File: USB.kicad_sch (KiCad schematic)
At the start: 34 parts, among them J1 USB_C_Receptable_USB2.0, U4 AP2141WG-7

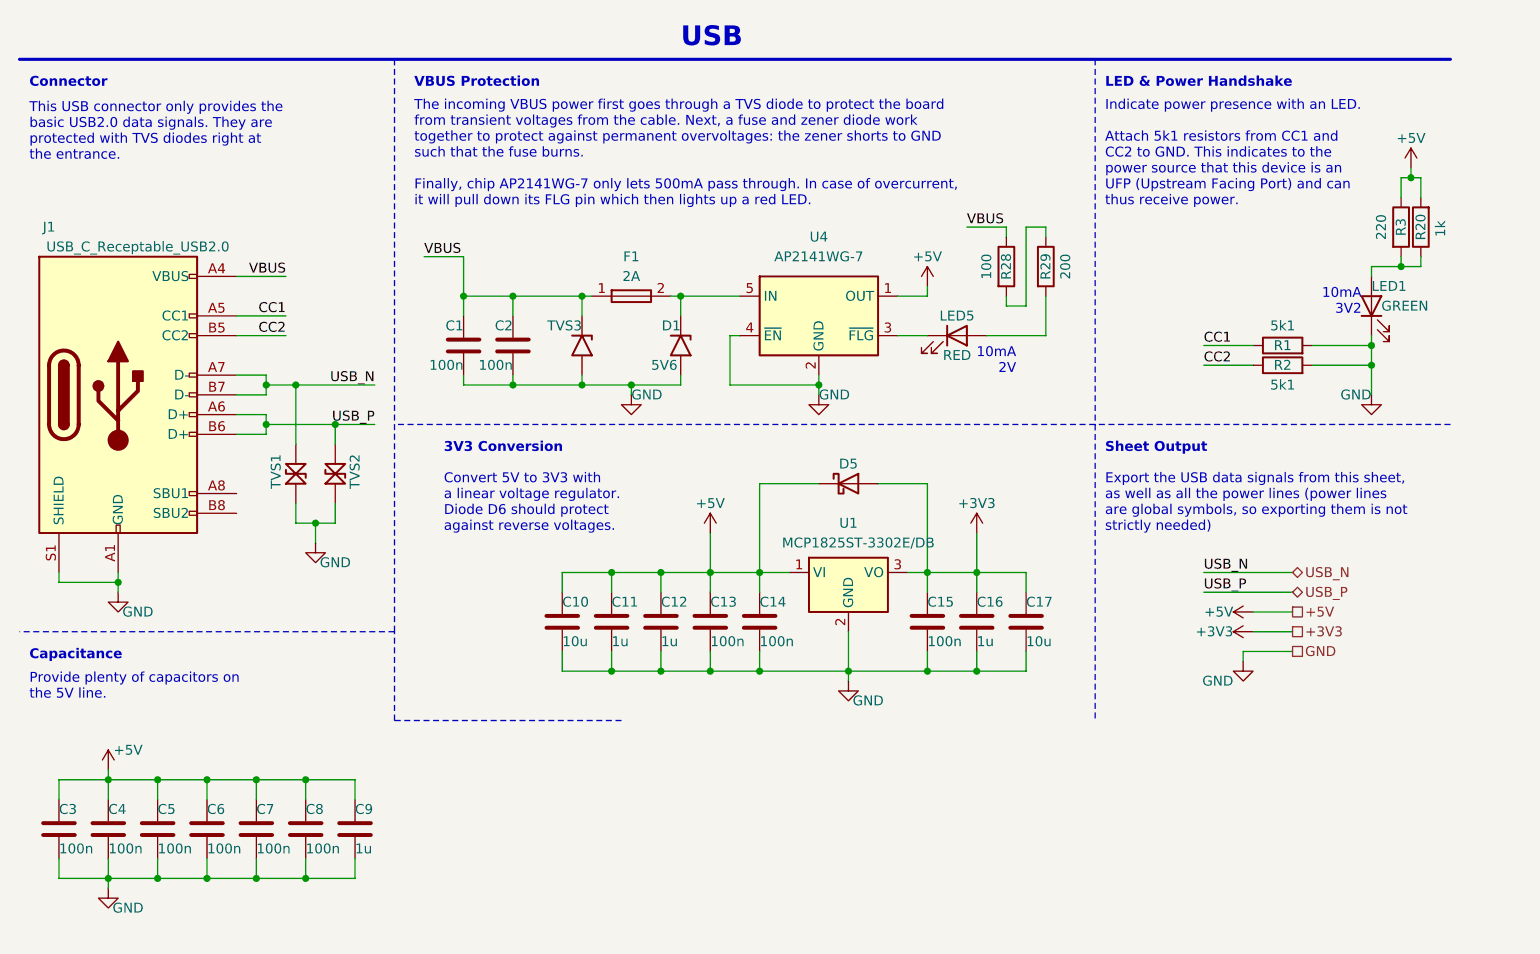
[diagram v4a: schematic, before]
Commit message: Renumber designators and draw new silkscreen
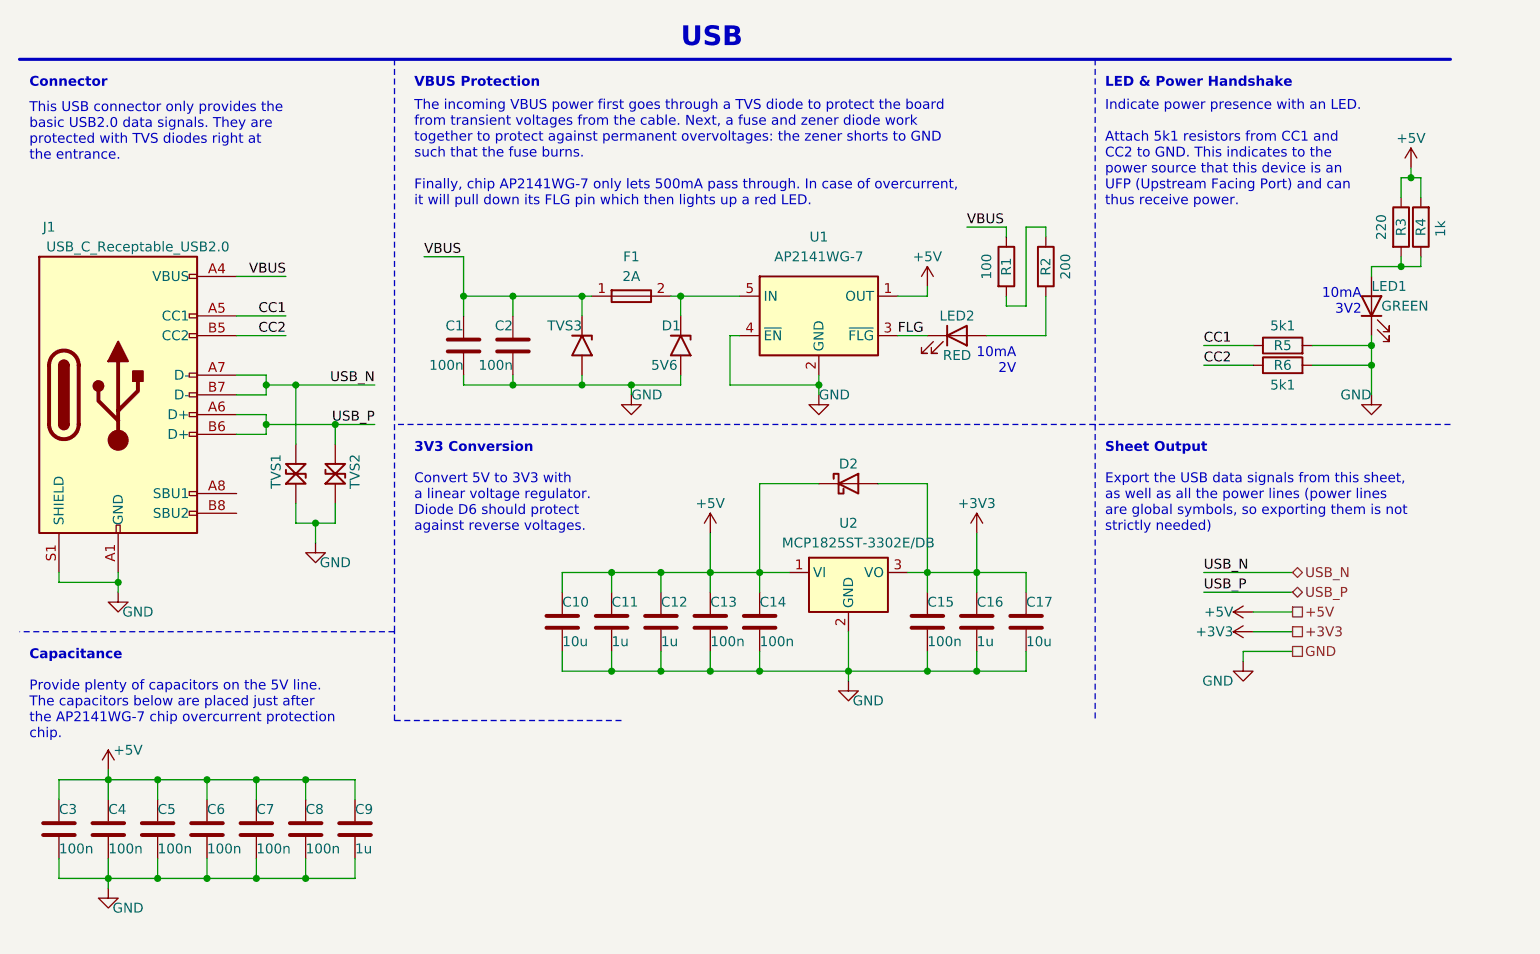
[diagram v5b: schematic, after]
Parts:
- renumbered D5 to D2, LED5 to LED2, R28 to R1, R29 to R2, R20 to R4, R1 to R5, R2 to R6, U4 to U1, U1 to U2
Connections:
- net FLG: now reaches LED2.1 (K), U1.3 (~{FLG})
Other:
- note added: "Provide plenty of capacitors on the 5V line. The capacitors below are placed just after the AP2141WG-7 chip overcurrent protection chip."
- note removed: "Provide plenty of capacitors on the 5V line."
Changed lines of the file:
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@@
     (effects (font (size 2.54 2.54) (thickness 0.508) bold) (justify left bottom))
   )
-  (text "3V3 Conversion" (at 67.31 69.85 0)
+  (text "3V3 Conversion" (at 63.5 69.85 0)
     (effects (font (size 1.27 1.27) (thickness 0.254) bold) (justify left bottom))
   )
@@
   )
   (text "Convert 5V to 3V3 with\na linear voltage regulator.\nDiode D6 should protect\nagainst reverse voltages.\n"
-    (at 67.31 80.01 0)
+    (at 63.5 80.01 0)
     (effects (font (size 1.27 1.27)) (justify left bottom))
   )
@@
     (effects (font (size 1.27 1.27)) (justify left bottom))
   )
-  (text "Provide plenty of capacitors on\nthe 5V line.\n" (at 13.97 101.6 0)
+  (text "Provide plenty of capacitors on the 5V line.\nThe capacitors below are placed just after\nthe AP2141WG-7 chip overcurrent protection\nchip."
+    (at 13.97 106.68 0)
     (effects (font (size 1.27 1.27)) (justify left bottom))
   )
@@
     (effects (font (size 1.27 1.27)) (justify right bottom))
   )
+  (label "FLG" (at 125.73 54.61 0) (fields_autoplaced)
+    (effects (font (size 1.27 1.27)) (justify left bottom))
+  )
   (label "USB_N" (at 58.42 60.96 180) (fields_autoplaced)
     (effects (font (size 1.27 1.27)) (justify right bottom))
@@
   (symbol (lib_id "Tiny_Scarab:SD103AWS") (at 119.38 73.66 0) (unit 1)
     (in_bom yes) (on_board yes) (dnp no)
-    (property "Reference" "D5" (at 119.38 71.12 0)
+    (property "Reference" "D2" (at 119.38 71.12 0)
       (effects (font (size 1.27 1.27)))
     )
@@
       (project "tiny-scarab"
         (path "/156c5422-ee07-49a4-8263-a2dbd26b90bd/99c48f54-1f97-4ff9-8db4-28f0cf987802"
-          (reference "D5") (unit 1)
+          (reference "D2") (unit 1)
         )
       )
@@
   (symbol (lib_id "Device:R") (at 193.04 40.64 180) (unit 1)
     (in_bom yes) (on_board yes) (dnp no)
-    (property "Reference" "R20" (at 193.04 40.64 90)
+    (property "Reference" "R4" (at 193.04 40.64 90)
       (effects (font (size 1.27 1.27)))
     )
@@
       (project "tiny-scarab"
         (path "/156c5422-ee07-49a4-8263-a2dbd26b90bd/99c48f54-1f97-4ff9-8db4-28f0cf987802"
-          (reference "R20") (unit 1)
+          (reference "R4") (unit 1)
         )
       )
@@
   (symbol (lib_id "Device:R") (at 144.78 45.72 0) (unit 1)
     (in_bom yes) (on_board yes) (dnp no)
-    (property "Reference" "R29" (at 144.78 45.72 90)
+    (property "Reference" "R2" (at 144.78 45.72 90)
       (effects (font (size 1.27 1.27)))
     )
@@
       (project "tiny-scarab"
         (path "/156c5422-ee07-49a4-8263-a2dbd26b90bd/99c48f54-1f97-4ff9-8db4-28f0cf987802"
-          (reference "R29") (unit 1)
+          (reference "R2") (unit 1)
         )
       )
@@
   (symbol (lib_id "Device:R") (at 175.26 58.42 90) (unit 1)
     (in_bom yes) (on_board yes) (dnp no)
-    (property "Reference" "R2" (at 175.26 58.42 90)
+    (property "Reference" "R6" (at 175.26 58.42 90)
       (effects (font (size 1.27 1.27)))
     )
@@
       (project "tiny-scarab"
         (path "/156c5422-ee07-49a4-8263-a2dbd26b90bd/99c48f54-1f97-4ff9-8db4-28f0cf987802"
-          (reference "R2") (unit 1)
+          (reference "R6") (unit 1)
         )
       )
@@
   (symbol (lib_id "Device:R") (at 139.7 45.72 0) (unit 1)
     (in_bom yes) (on_board yes) (dnp no)
-    (property "Reference" "R28" (at 139.7 45.72 90)
+    (property "Reference" "R1" (at 139.7 45.72 90)
       (effects (font (size 1.27 1.27)))
     )
@@
       (project "tiny-scarab"
         (path "/156c5422-ee07-49a4-8263-a2dbd26b90bd/99c48f54-1f97-4ff9-8db4-28f0cf987802"
-          (reference "R28") (unit 1)
+          (reference "R1") (unit 1)
         )
       )
@@
   (symbol (lib_id "Tiny_Scarab:AP2141WG-7") (at 115.57 52.07 0) (unit 1)
     (in_bom yes) (on_board yes) (dnp no) (fields_autoplaced)
-    (property "Reference" "U4" (at 115.57 41.91 0)
+    (property "Reference" "U1" (at 115.57 41.91 0)
       (effects (font (size 1.27 1.27)))
     )
@@
       (project "tiny-scarab"
         (path "/156c5422-ee07-49a4-8263-a2dbd26b90bd/99c48f54-1f97-4ff9-8db4-28f0cf987802"
-          (reference "U4") (unit 1)
+          (reference "U1") (unit 1)
         )
       )
@@
   (symbol (lib_id "Device:R") (at 175.26 55.88 90) (unit 1)
     (in_bom yes) (on_board yes) (dnp no)
-    (property "Reference" "R1" (at 175.26 55.88 90)
+    (property "Reference" "R5" (at 175.26 55.88 90)
       (effects (font (size 1.27 1.27)))
     )
@@
       (project "tiny-scarab"
         (path "/156c5422-ee07-49a4-8263-a2dbd26b90bd/99c48f54-1f97-4ff9-8db4-28f0cf987802"
-          (reference "R1") (unit 1)
+          (reference "R5") (unit 1)
         )
       )
@@
   (symbol (lib_id "Tiny_Scarab:LED_RED_CSL0902UT") (at 133.35 54.61 0) (unit 1)
     (in_bom yes) (on_board yes) (dnp no)
-    (property "Reference" "LED5" (at 133.35 52.07 0)
+    (property "Reference" "LED2" (at 133.35 52.07 0)
       (effects (font (size 1.27 1.27)))
     )
@@
       (project "tiny-scarab"
         (path "/156c5422-ee07-49a4-8263-a2dbd26b90bd/99c48f54-1f97-4ff9-8db4-28f0cf987802"
-          (reference "LED5") (unit 1)
+          (reference "LED2") (unit 1)
         )
       )
@@
   (symbol (lib_id "Tiny_Scarab:MCP1825ST-3302E/DB") (at 119.38 85.09 0) (unit 1)
     (in_bom yes) (on_board yes) (dnp no)
-    (property "Reference" "U1" (at 119.38 78.74 0)
+    (property "Reference" "U2" (at 119.38 78.74 0)
       (effects (font (size 1.27 1.27)))
     )
@@
       (project "tiny-scarab"
         (path "/156c5422-ee07-49a4-8263-a2dbd26b90bd/99c48f54-1f97-4ff9-8db4-28f0cf987802"
-          (reference "U1") (unit 1)
-        )
-      )
+          (reference "U2") (unit 1)
+        )
+      )

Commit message: Replace TVS diodes with cheaper alternative
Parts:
- TVS1, TVS2: SPN CDSOD323-T05LCTR-ND -> (none); Supplier DigiKey -> (none)
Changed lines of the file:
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@@
       (effects (font (size 1.27 1.27)) (justify left bottom) hide)
-    )
-    (property "Supplier" "DigiKey" (at 58.42 77.47 0)
-      (effects (font (size 1.27 1.27)) (justify left) hide)
-    )
-    (property "SPN" "CDSOD323-T05LCTR-ND" (at 58.42 80.01 0)
-      (effects (font (size 1.27 1.27)) (justify left) hide)
     )
     (property "JLCPCB Part #" "C840637" (at 48.26 72.39 0)
@@
       (effects (font (size 1.27 1.27)) (justify left bottom) hide)
     )
-    (property "Supplier" "DigiKey" (at 63.5 77.47 0)
-      (effects (font (size 1.27 1.27)) (justify left) hide)
-    )
-    (property "SPN" "CDSOD323-T05LCTR-ND" (at 63.5 80.01 0)
-      (effects (font (size 1.27 1.27)) (justify left) hide)
-    )
     (property "JLCPCB Part #" "C840637" (at 53.34 72.39 0)

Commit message: Clean up symbols library
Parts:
- D1: DigiKey (none) -> 3372-1SMA4734ATR-ND; Mouser (none) -> 241-1SMA4734AUR1000A
- D2: DigiKey (none) -> 4530-SD103AWSTR-ND; Farnell (none) -> 2393466; Manufacturer ANBON SEMICONDUCTOR (INT'L) LIMITED -> AnBon Semiconductor; Mouser (none) -> 78-SD103AWS-E3-08
- F1: DigiKey (none) -> 749-MFU0603FF02000P500TR-ND; Farnell (none) -> 4247180; Mouser (none) -> 594-MFU0603-FF-2.0
- LED1: DigiKey (none) -> 846-CSL0902ET1TR-ND
- LED2: DigiKey (none) -> 846-CSL0902UT1TR-ND
- TVS1, TVS2: Farnell (none) -> 1824861; Mouser (none) -> 652-CDSOD323-T05LC
- TVS3: DigiKey (none) -> SMAJ5.0ALFTR-ND; Farnell (none) -> 1827607; Mouser (none) -> 576-SMAJ5.0A
- U1: DigiKey (none) -> AP2141WGDITR-ND; Farnell (none) -> 3482799; Mouser (none) -> 621-AP2141WG-7
- U2: DigiKey (none) -> MCP1825ST-3302E/DBTR-ND; Farnell (none) -> 2857611; Mouser (none) -> 579-MCP1825ST3302EDB
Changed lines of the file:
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@@
       (effects (font (size 1.27 1.27)) hide)
     )
-    (property "Manufacturer" "ANBON SEMICONDUCTOR (INT'L) LIMITED" (at 119.38 58.42 0)
+    (property "Manufacturer" "AnBon Semiconductor" (at 119.38 58.42 0)
       (effects (font (size 1.27 1.27)) hide)
     )
@@
     )
     (property "JLCPCB Part #" "C397613" (at 119.38 73.66 0)
+      (effects (font (size 1.27 1.27)) hide)
+    )
+    (property "DigiKey" "4530-SD103AWSTR-ND" (at 119.38 62.23 0)
+      (effects (font (size 1.27 1.27)) hide)
+    )
+    (property "Farnell" "2393466" (at 119.38 64.77 0)
+      (effects (font (size 1.27 1.27)) hide)
+    )
+    (property "Mouser" "78-SD103AWS-E3-08" (at 119.38 67.31 0)
       (effects (font (size 1.27 1.27)) hide)
     )
@@
       (effects (font (size 1.27 1.27)) (justify left) hide)
     )
+    (property "Farnell" "1824861" (at 48.26 58.42 0)
+      (effects (font (size 1.27 1.27)) hide)
+    )
+    (property "Mouser" "652-CDSOD323-T05LC" (at 48.26 60.96 0)
+      (effects (font (size 1.27 1.27)) hide)
+    )
     (pin "2")
     (pin "1")
@@
       (effects (font (size 1.27 1.27)) hide)
     )
-    (property "Datasheet" "" (at 25.4 21.59 0)
+    (property "Datasheet" "https://datasheet.lcsc.com/lcsc/2201121330_DEALON-USB-TYPE-C-018_C2927038.pdf" (at 25.4 21.59 0)
       (effects (font (size 1.27 1.27)) hide)
     )
@@
     )
     (property "JLCPCB Part #" "C2927038" (at 25.4 41.91 0)
+      (effects (font (size 1.27 1.27)) hide)
+    )
+    (property "DigiKey" "" (at 25.4 62.23 0)
+      (effects (font (size 1.27 1.27)) hide)
+    )
+    (property "Farnell" "" (at 25.4 62.23 0)
+      (effects (font (size 1.27 1.27)) hide)
+    )
+    (property "Mouser" "" (at 25.4 62.23 0)
       (effects (font (size 1.27 1.27)) hide)
     )
@@
       (effects (font (size 1.27 1.27)) hide)
     )
+    (property "DigiKey" "749-MFU0603FF02000P500TR-ND" (at 91.44 34.29 0)
+      (effects (font (size 1.27 1.27)) hide)
+    )
+    (property "Farnell" "4247180" (at 91.44 36.83 0)
+      (effects (font (size 1.27 1.27)) hide)
+    )
+    (property "Mouser" "594-MFU0603-FF-2.0" (at 91.44 39.37 0)
+      (effects (font (size 1.27 1.27)) hide)
+    )
     (pin "1")
     (pin "2")
@@
       (effects (font (size 1.27 1.27)) hide)
     )
+    (property "DigiKey" "3372-1SMA4734ATR-ND" (at 110.49 55.88 0)
+      (effects (font (size 1.27 1.27)) hide)
+    )
+    (property "Farnell" "" (at 97.79 55.88 0)
+      (effects (font (size 1.27 1.27)) hide)
+    )
+    (property "Mouser" "241-1SMA4734AUR1000A" (at 107.95 55.88 0)
+      (effects (font (size 1.27 1.27)) hide)
+    )
     (pin "1")
     (pin "2")
@@
     )
     (property "Farnell" "4129807" (at 181.61 50.8 0)
+      (effects (font (size 1.27 1.27)) hide)
+    )
+    (property "DigiKey" "846-CSL0902ET1TR-ND" (at 173.99 50.8 0)
       (effects (font (size 1.27 1.27)) hide)
     )
@@
       (effects (font (size 1.27 1.27)) hide)
     )
+    (property "DigiKey" "AP2141WGDITR-ND" (at 115.57 33.02 0)
+      (effects (font (size 1.27 1.27)) hide)
+    )
+    (property "Farnell" "3482799" (at 115.57 35.56 0)
+      (effects (font (size 1.27 1.27)) hide)
+    )
+    (property "Mouser" "621-AP2141WG-7" (at 115.57 38.1 0)
+      (effects (font (size 1.27 1.27)) hide)
+    )
     (pin "2")
     (pin "4")
@@
       (effects (font (size 1.27 1.27)) hide)
     )
+    (property "DigiKey" "SMAJ5.0ALFTR-ND" (at 97.79 55.88 0)
+      (effects (font (size 1.27 1.27)) hide)
+    )
+    (property "Farnell" "1827607" (at 95.25 55.88 0)
+      (effects (font (size 1.27 1.27)) hide)
+    )
+    (property "Mouser" "576-SMAJ5.0A" (at 92.71 55.88 0)
+      (effects (font (size 1.27 1.27)) hide)
+    )
     (pin "1")
     (pin "2")
@@
       (effects (font (size 1.27 1.27)) (justify left) hide)
     )
+    (property "Farnell" "1824861" (at 53.34 58.42 0)
+      (effects (font (size 1.27 1.27)) hide)
+    )
+    (property "Mouser" "652-CDSOD323-T05LC" (at 53.34 60.96 0)
+      (effects (font (size 1.27 1.27)) hide)
+    )
     (pin "2")
     (pin "1")
@@
       (effects (font (size 1.27 1.27)) hide)
     )
+    (property "DigiKey" "846-CSL0902UT1TR-ND" (at 133.35 41.91 0)
+      (effects (font (size 1.27 1.27)) hide)
+    )
     (pin "2")
     (pin "1")
@@
       (effects (font (size 1.27 1.27)) hide)
     )
+    (property "DigiKey" "MCP1825ST-3302E/DBTR-ND" (at 119.38 69.85 0)
+      (effects (font (size 1.27 1.27)) hide)
+    )
+    (property "Farnell" "2857611" (at 119.38 72.39 0)
+      (effects (font (size 1.27 1.27)) hide)
+    )
+    (property "Mouser" "579-MCP1825ST3302EDB" (at 119.38 74.93 0)
+      (effects (font (size 1.27 1.27)) hide)
+    )
